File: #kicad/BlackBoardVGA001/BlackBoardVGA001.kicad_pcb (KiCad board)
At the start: 2 copper layers, 72.5 x 85.1 mm, 29 parts, among them J1 VGA, J2 PS/2, J3 Left, J4 Right, J5 LAN8720

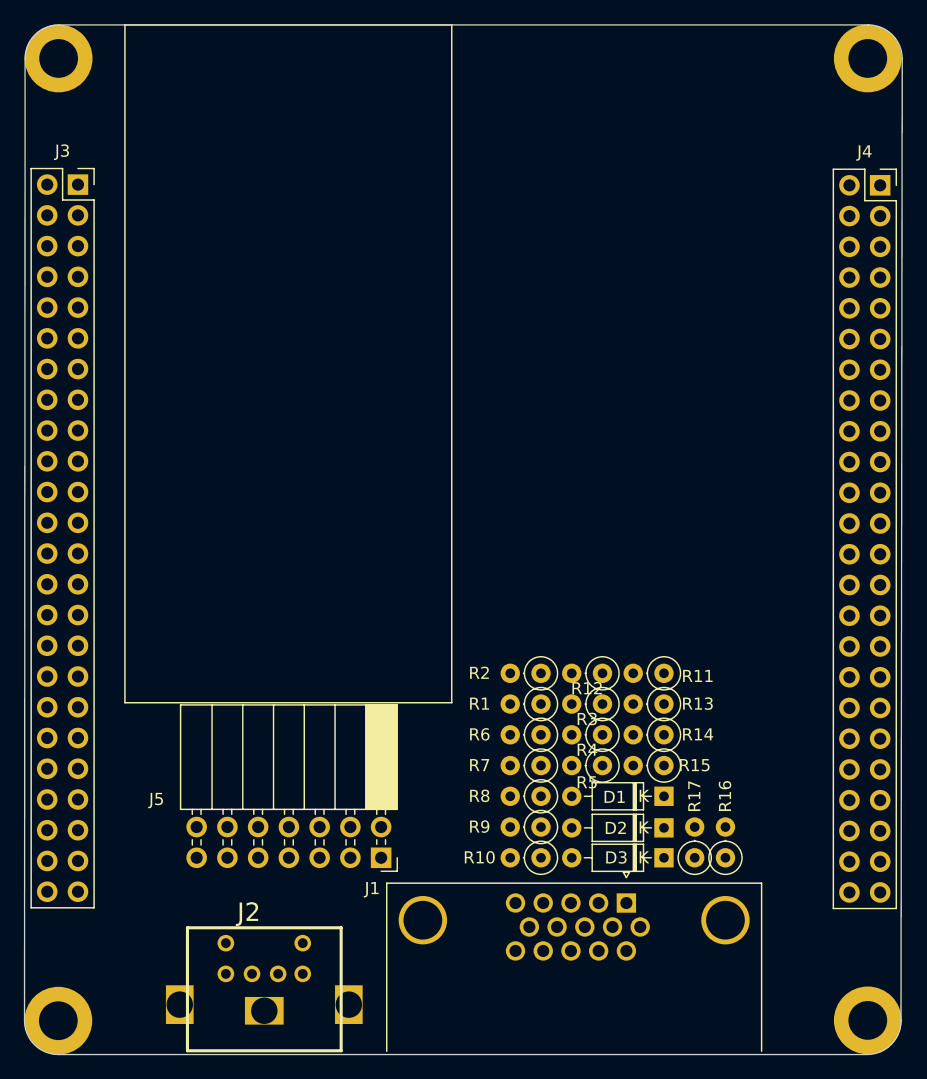
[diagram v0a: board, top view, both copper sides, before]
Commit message: added a second ps2 connector, eventually for mouse (not connected to any gpio yet)
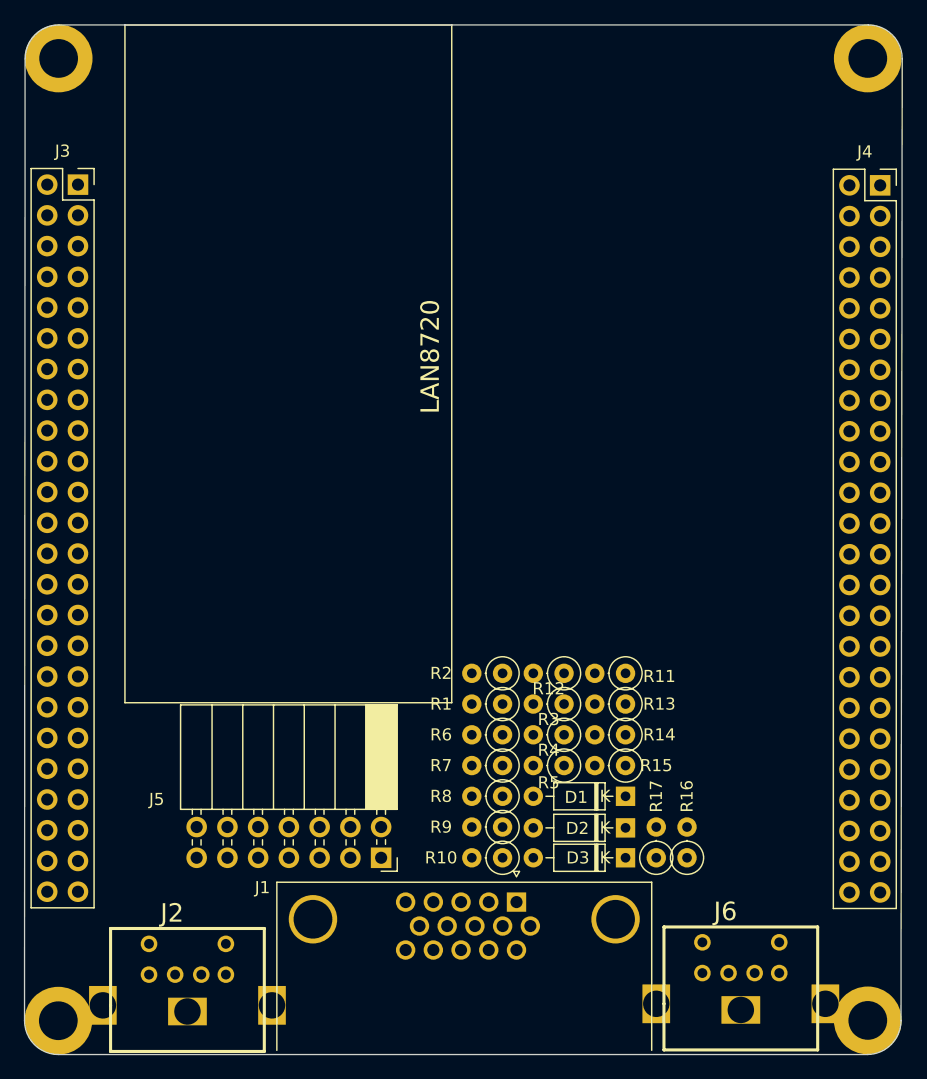
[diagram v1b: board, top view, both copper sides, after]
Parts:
- added J6: PS/2, BlackBoardVGA001:Mini_din6, F.Cu at (100.3, 137.8)
- moved J1 9.08 mm to (81.8, 130.7)
- moved J2 6.35 mm to (54.6, 137.9)
- moved R12 3.18 mm to (85.7, 111.8)
- moved R3 3.18 mm to (85.7, 114.3)
- moved R4 3.18 mm to (85.7, 116.8)
- moved R5 3.18 mm to (85.7, 119.4)
- moved D1 3.17 mm to (90.8, 121.9)
- moved D2 3.17 mm to (90.8, 124.5)
- moved D3 3.17 mm to (90.8, 127.0)
- moved R1 3.17 mm to (80.6, 114.3)
- moved R10 3.17 mm to (80.6, 127.0)
- moved R11 3.17 mm to (90.8, 111.8)
- moved R13 3.17 mm to (90.8, 114.3)
- moved R14 3.17 mm to (90.8, 116.8)
- moved R15 3.17 mm to (90.8, 119.4)
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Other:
- board text added: "LAN8720"
